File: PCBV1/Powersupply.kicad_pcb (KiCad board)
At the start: 4 copper layers, 145 x 99.1 mm, 136 parts, among them J1 Conn_01x02, J2 Conn_WallPlug, J3 QSH-030-01-F-D-A-K-TR, J4 M50-3610742, J5 Conn_01x02, J6 Conn_01x02, J7 Conn_01x02, J8 Conn_01x07, J9 Conn_01x03, T1 EFD 20/10/7, U1 ST1S41PHR, U2 ST1S41PHR, U3 VIPER318HDTR, U4 STM32F469IITx, U5 IS42S16400J-xT, U6 W25Q32JVSS, X1 ECS-5032MV-100-CN-TR

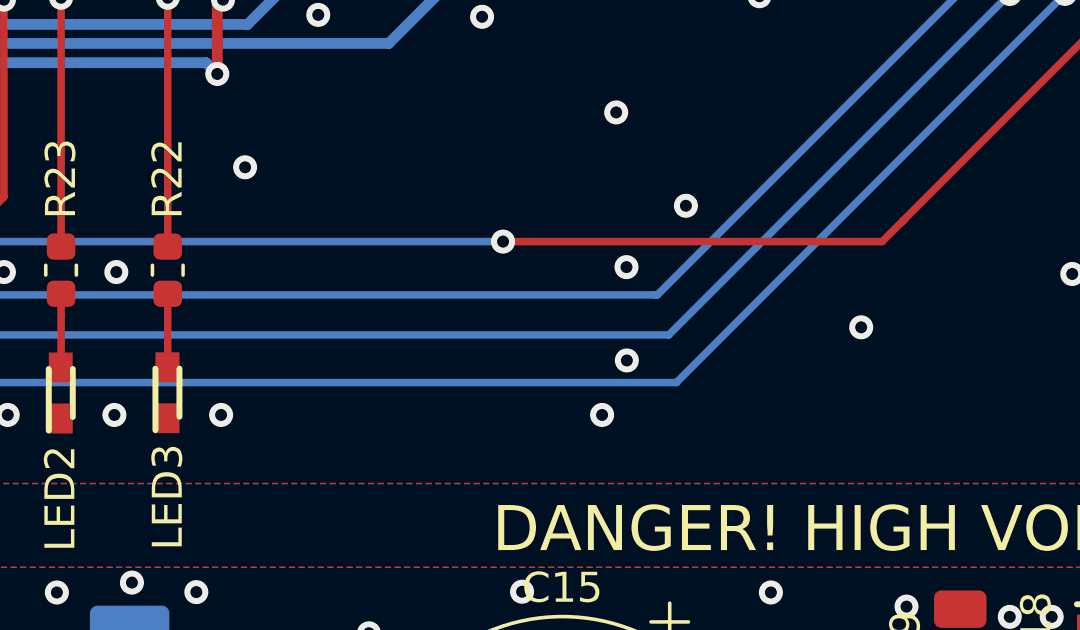
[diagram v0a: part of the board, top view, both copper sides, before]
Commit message: Added silk screen text.
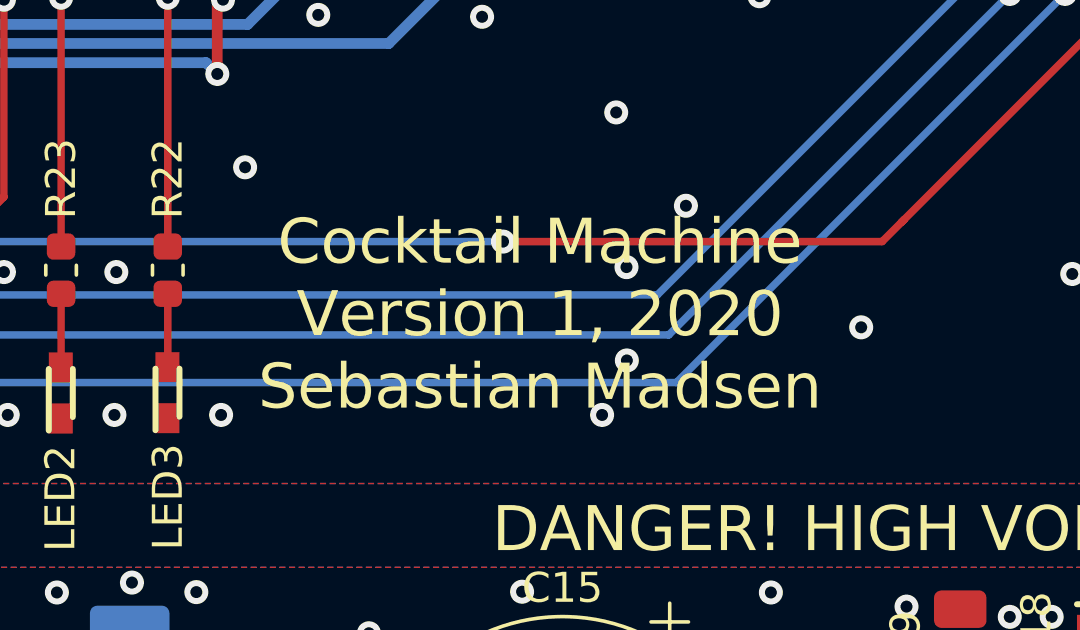
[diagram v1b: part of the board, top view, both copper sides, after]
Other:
- board text added: "Cocktail Machine Version 1, 2020 Sebastian Madsen"

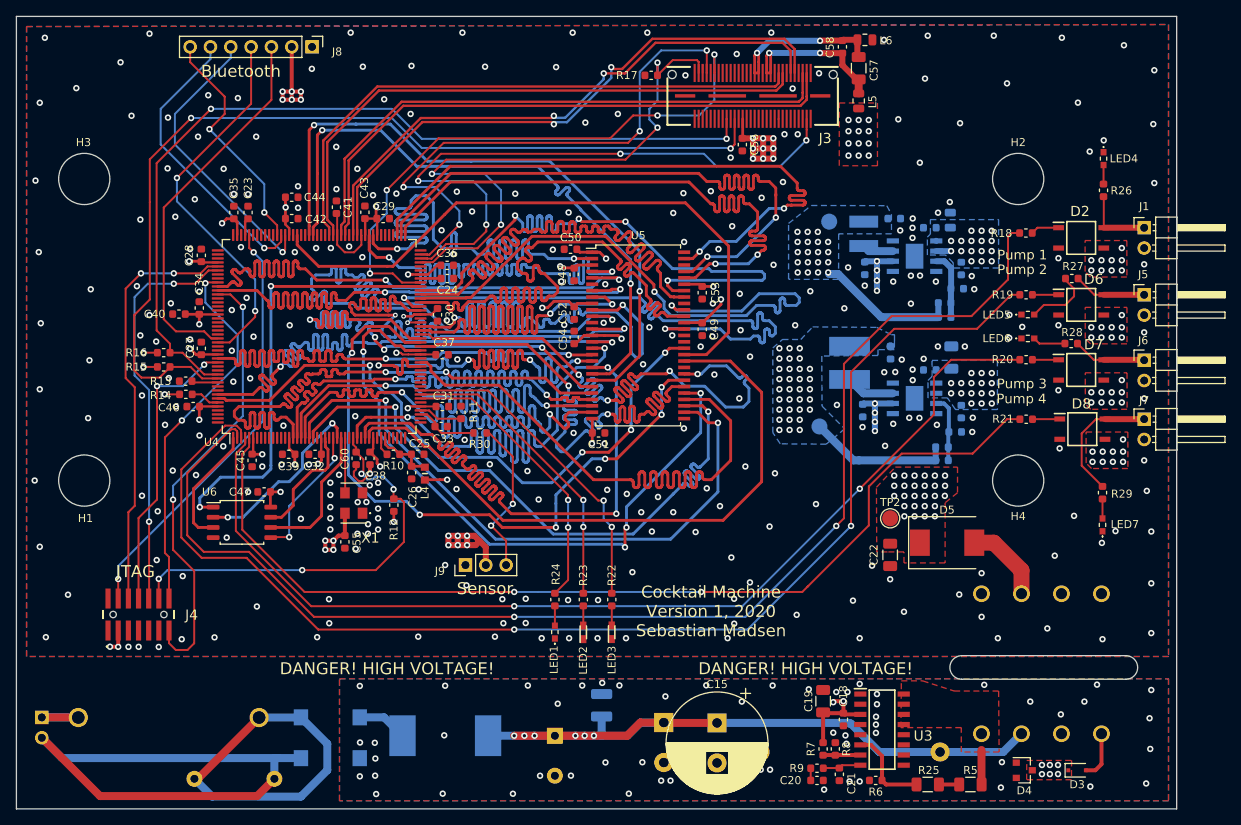
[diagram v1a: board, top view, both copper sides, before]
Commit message: Prettified the PCB, minor changes to routing.
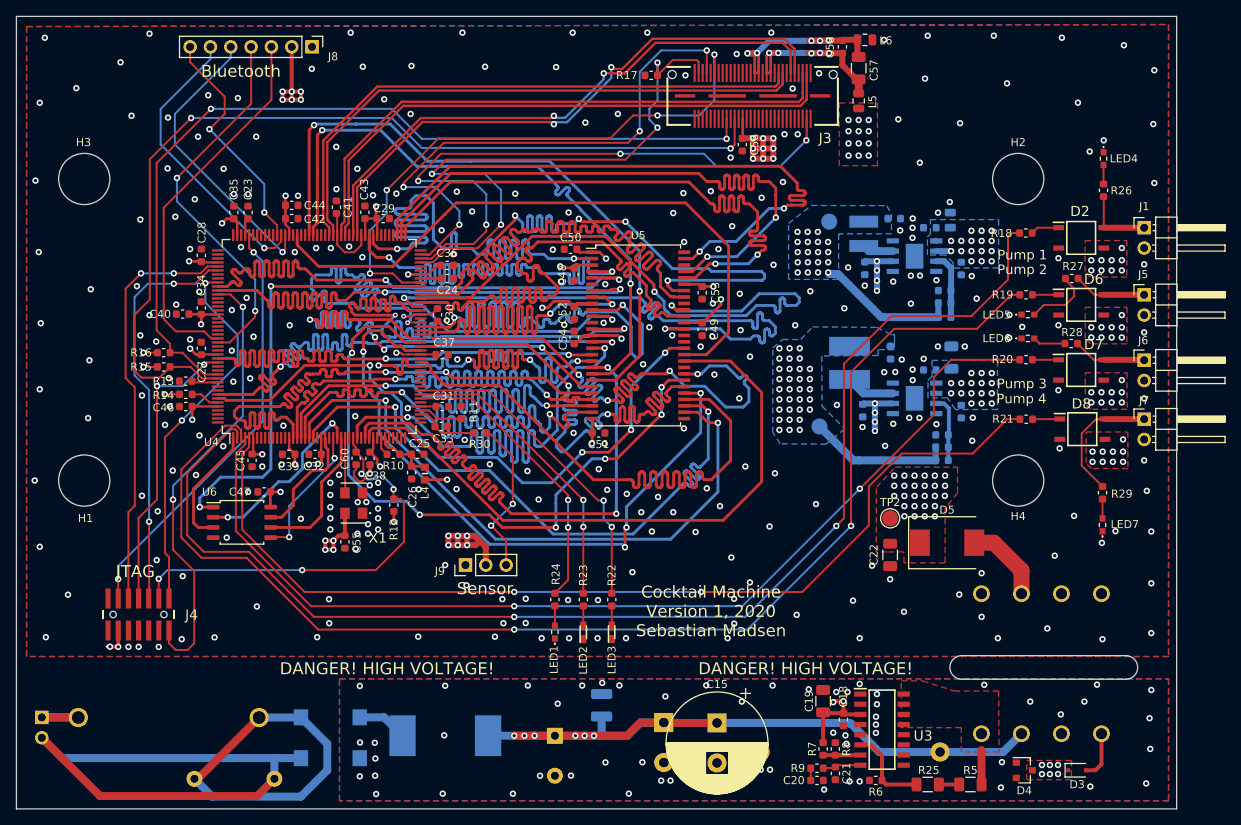
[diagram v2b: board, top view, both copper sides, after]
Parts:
- moved R2 1.69 mm to (199.5, 70.1), turned to 180 degrees
- moved R4 1.59 mm to (199.8, 52.0), turned to 180 degrees
- moved C44 1.01 mm to (118.2, 41.4)
- moved C46 0.92 mm to (105.0, 66.5)
- moved C21 0.50 mm to (186.2, 112.4)
- moved C40 0.46 mm to (104.6, 55.0)
- moved C34 0.25 mm to (106.9, 54.2)
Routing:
- net Net-(C57-Pad2): track 21.1 -> 26.1 mm, vias 2 -> 5
- net Net-(C57-Pad1): track 20.9 -> 24.7 mm, vias 2 -> 5
- net 3V3: track 191.0 -> 191.7 mm
- net GND: vias 284 -> 283

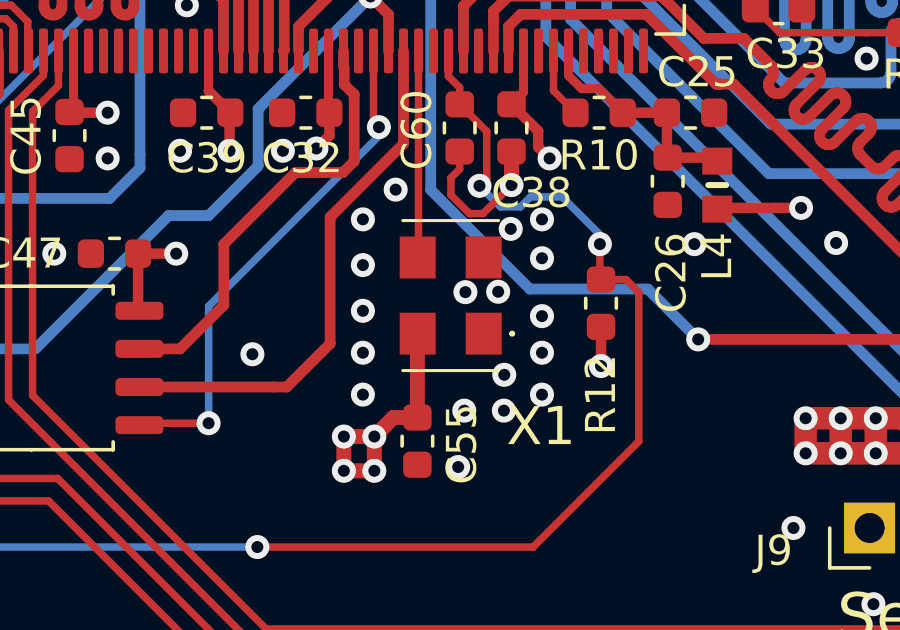
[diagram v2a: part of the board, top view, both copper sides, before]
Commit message: Removed guard ring from crystal.
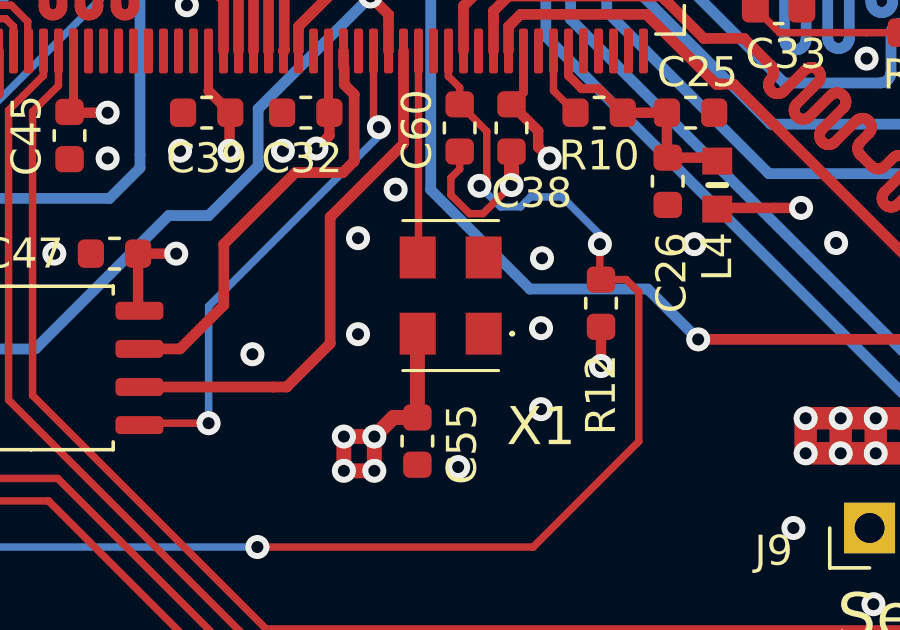
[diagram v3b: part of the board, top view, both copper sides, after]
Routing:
- net GND: track 5.45 -> 5.44 mm, vias 283 -> 272
